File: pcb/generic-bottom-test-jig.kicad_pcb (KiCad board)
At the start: 2 copper layers, 36 x 36 mm, 13 parts

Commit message: Gerbers for v1 of the test jig.
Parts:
- removed PORT_ANDOR1: SN74LVC1G0832, Housings_SOT-23_SOT-143_TSOT-6:SC-70-6_Handsoldering
- removed PORT_C1: 0.1uF, Capacitors_SMD:C_0603_HandSoldering
- removed PORT_IC1: AT24CS02-MAHM, Housings_DFN_QFN:DFN-8-1EP_3x2mm_Pitch0.5mm
- removed PORT_IN1: DF40-80pin-Header, DF40-80pin-Header
- removed PORT_INV1, PORT_XOR1: SN74LVC1G58, Housings_SOT-23_SOT-143_TSOT-6:SC-70-6_Handsoldering
- removed PORT_P1: CONN_01X01, Measurement_Points:Measurement_Point_Round-SMD-Pad_Small
- removed PORT_R1: 10k, Resistors_SMD:R_0603_HandSoldering
- added C1: 2.2uF, Capacitors_SMD:C_0603_HandSoldering, F.Cu at (110.6, 106.4)
- added C2: 1uF, Capacitors_SMD:C_0603_HandSoldering, F.Cu at (116.9, 106.4)
- added CON1: BARREL_JACK, barrel-jack:PJ-037BH-SMT, F.Cu at (116.5, 118.5)
- added D1: RED, LEDs:LED_0603, F.Cu at (125.2, 134.3)
- added D2: YELLOW, LEDs:LED_0603, F.Cu at (125.2, 130.8)
- added D3: GREEN, LEDs:LED_0603, F.Cu at (125.2, 127.3)
- added G***: Chickadee 3mm, chickadee:chickadee_3mm_fcu, F.Cu at (159.9, 129.2)
- added G***: LOGO, flightstack:flightstack-12mm, F.Cu at (190.6, 129.5)
- added P1: CONN_01X06, Pin_Headers:Pin_Header_Straight_1x06, F.Cu at (111.1, 138.6)
- added P10: CONN_01X01, Measurement_Points:Measurement_Point_Round-TH_Small, F.Cu at (120.6, 106.3)
- added P11: CONN_01X01, Measurement_Points:Measurement_Point_Square-TH_Small, F.Cu at (119.2, 111.0)
- added P2: CONN_02X25, Pin_Headers:Pin_Header_Straight_2x25, F.Cu at (134.0, 138.6)
- added P3: CONN_01X04, Pin_Headers:Pin_Header_Straight_1x04, F.Cu at (117.2, 97.2)
- added P4: CONN_02X25, Pin_Headers:Pin_Header_Straight_2x25, F.Cu at (134.0, 87.8)
- added P5: CONN_01X16, fci:SFW12LF-16pin, F.Cu at (144.5, 130.0)
- added P6: CONN_02X10, hirose-df40:DF40-1.5mm-20pin-Receptacle, F.Cu at (190.2, 108.0)
- added P7: CONN_01X01, mill-max-pogo-pin:0910, F.Cu at (158.6, 91.2)
- added P8: CONN_01X16, fci:SFW12LF-16pin, F.Cu at (175.0, 130.0)
- added P9: CONN_01X01, Measurement_Points:Measurement_Point_Round-TH_Small, F.Cu at (117.8, 101.8)
- added Q1: Q_NMOS_GSD, TO_SOT_Packages_SMD:SOT-23_Handsoldering, F.Cu at (115.0, 111.0)
- added R1: 1k, Resistors_SMD:R_0603_HandSoldering, F.Cu at (120.3, 134.3)
- added R2: 1k, Resistors_SMD:R_0603_HandSoldering, F.Cu at (120.3, 130.8)
- added R3: 1k, Resistors_SMD:R_0603_HandSoldering, F.Cu at (120.3, 127.3)
- added R4: 0, Resistors_SMD:R_0603_HandSoldering, B.Cu at (118.7, 132.8)
- added R5: 0, Resistors_SMD:R_0603_HandSoldering, B.Cu at (113.6, 132.8)
- added REF**: MountingHole_3mm, Mounting_Holes:MountingHole_3mm, F.Cu at (193.8, 123.2)
- added REF**: MountingHole_3mm, Mounting_Holes:MountingHole_3mm, F.Cu at (193.8, 92.8)
- added SW1: Switch_SPDT_x2, copal-electronics:CL-SB-22B, F.Cu at (113.3, 89.0)
- added SW2: SPST, Buttons_Switches_SMD:SW_SPST_PTS645, F.Cu at (114.0, 130.2)
- added U1: STMPS2151, TO_SOT_Packages_SMD:SOT-23-5, F.Cu at (113.8, 101.8)
- added U2: TLV70233DBV, TO_SOT_Packages_SMD:SOT-23-5, F.Cu at (113.7, 106.3)
- PORT_OUT1: value DF40-3-4mm-80pin-Receptacle -> CKD_SANDWICH; footprint DF40-3-4mm-80pin-Receptacle -> hirose-df40:DF40-3-4mm-80pin-Receptacle
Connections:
- PORT_OUT1 pad 1: (no net) -> /PD5
- PORT_OUT1 pad 10: (no net) -> /PC15
- PORT_OUT1 pad 11: (no net) -> /PB7_SDA
- PORT_OUT1 pad 12: (no net) -> /PB6_SCL
- PORT_OUT1 pad 13: (no net) -> /PF0
- PORT_OUT1 pad 14: (no net) -> /PF1
- PORT_OUT1 pad 15: (no net) -> /PF9
- PORT_OUT1 pad 16: (no net) -> /PC0_3V3
- PORT_OUT1 pad 17: (no net) -> /PC1_3V3_E
- PORT_OUT1 pad 18: (no net) -> /PC2_BATT
- PORT_OUT1 pad 19: (no net) -> /PF10_5V
- PORT_OUT1 pad 2: (no net) -> /PD7
- PORT_OUT1 pad 20: (no net) -> /PF10_5V
- PORT_OUT1 pad 21: (no net) -> /PF10_5V
- PORT_OUT1 pad 22: (no net) -> /PF10_5V
- PORT_OUT1 pad 23: (no net) -> /PF10_5V
- PORT_OUT1 pad 24: (no net) -> /PF10_5V
- PORT_OUT1 pad 25: (no net) -> /PC3_SWITCH
- PORT_OUT1 pad 26: (no net) -> /PF2
- PORT_OUT1 pad 27: (no net) -> /PA1
- PORT_OUT1 pad 28: (no net) -> /PA3
- PORT_OUT1 pad 29: (no net) -> /PA2
- PORT_OUT1 pad 3: (no net) -> /PB4
- PORT_OUT1 pad 30: (no net) -> /PF4
- PORT_OUT1 pad 31: (no net) -> /PA5_SCL
- PORT_OUT1 pad 32: (no net) -> /PA4
- PORT_OUT1 pad 33: (no net) -> /PA7_SDA
- PORT_OUT1 pad 34: (no net) -> /PA6_SDO
- PORT_OUT1 pad 35: (no net) -> /PC5
- PORT_OUT1 pad 36: (no net) -> /PC4
- PORT_OUT1 pad 37: (no net) -> /PB0
- PORT_OUT1 pad 38: (no net) -> /PB1
- PORT_OUT1 pad 39: (no net) -> /PB2
- PORT_OUT1 pad 4: (no net) -> /PB5
- PORT_OUT1 pad 40: (no net) -> /PE7
- PORT_OUT1 pad 41: (no net) -> /PD6
- PORT_OUT1 pad 42: (no net) -> /PD3
- PORT_OUT1 pad 43: (no net) -> /PD4
- PORT_OUT1 pad 44: (no net) -> /PD1
- PORT_OUT1 pad 45: (no net) -> /PD2
- PORT_OUT1 pad 46: (no net) -> /PC12
- PORT_OUT1 pad 47: (no net) -> /PD0
- PORT_OUT1 pad 48: (no net) -> /PC10
- PORT_OUT1 pad 49: (no net) -> /PC11
- PORT_OUT1 pad 5: (no net) -> /PB8
- PORT_OUT1 pad 50: (no net) -> /PA14_SWCLK
- PORT_OUT1 pad 51: (no net) -> /PA15
- PORT_OUT1 pad 52: (no net) -> /PF6
- PORT_OUT1 pad 53: (no net) -> /PA10
- PORT_OUT1 pad 54: (no net) -> /PA9
- PORT_OUT1 pad 55: (no net) -> /PA8
- PORT_OUT1 pad 56: (no net) -> /PC9
- PORT_OUT1 pad 57: (no net) -> /PC8_GND
- PORT_OUT1 pad 58: (no net) -> /PC8_GND
- PORT_OUT1 pad 59: (no net) -> /PC8_GND
- PORT_OUT1 pad 6: (no net) -> /PB9
- PORT_OUT1 pad 60: (no net) -> /PC8_GND
- PORT_OUT1 pad 61: (no net) -> /PC8_GND
- PORT_OUT1 pad 62: (no net) -> /PC8_GND
- PORT_OUT1 pad 63: (no net) -> /PC8_GND
- PORT_OUT1 pad 64: (no net) -> /PC8_GND
- PORT_OUT1 pad 65: (no net) -> /PC6_BOOT0
- PORT_OUT1 pad 66: (no net) -> /PC7_RESET
- PORT_OUT1 pad 67: (no net) -> /PD15
- PORT_OUT1 pad 68: (no net) -> /PD14
- PORT_OUT1 pad 69: (no net) -> /PD13
- PORT_OUT1 pad 7: (no net) -> /PE6
- PORT_OUT1 pad 70: (no net) -> /PD12
- PORT_OUT1 pad 71: (no net) -> /PD11
- PORT_OUT1 pad 72: (no net) -> /PD10
- PORT_OUT1 pad 73: (no net) -> /PD9_RX
- PORT_OUT1 pad 74: (no net) -> /PD8_TX
- PORT_OUT1 pad 75: (no net) -> /PB15
- PORT_OUT1 pad 76: (no net) -> /PB14
- PORT_OUT1 pad 77: (no net) -> /PB13
- PORT_OUT1 pad 78: (no net) -> /PB12
- PORT_OUT1 pad 79: (no net) -> /PB11
- PORT_OUT1 pad 8: (no net) -> /PC13
- PORT_OUT1 pad 80: (no net) -> /PB10
- PORT_OUT1 pad 9: (no net) -> /PC14
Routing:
- net (no net): track 470.7 -> 0.07 mm, vias 78 -> 0
- net /PC8_GND: track 0.00 -> 157.4 mm, vias 0 -> 2
- net /PF10_5V: track 0.00 -> 131.7 mm, vias 0 -> 4
- net /PC7_RESET: track 0.00 -> 126.9 mm, vias 0 -> 6
- net /PC0_3V3: track 0.00 -> 98.9 mm, vias 0 -> 1
- net /PE9_LD3_RED: track 0.00 -> 93.2 mm, vias 0 -> 4
- net /PC6_BOOT0: track 0.00 -> 86.0 mm, vias 0 -> 4
- net +5V: track 0.00 -> 85.5 mm, vias 0 -> 4
- net /PA13_SWDIO: track 0.00 -> 82.4 mm, vias 0 -> 1
- net /PC3_SWITCH: track 0.00 -> 78.5 mm, vias 0 -> 2
- net /SWCLK: track 0.00 -> 78.2 mm, vias 0 -> 7
- net /PE11_LD7_GREEN: track 0.00 -> 71.3 mm, vias 0 -> 3
- net /SWDIO: track 0.00 -> 70.4 mm, vias 0 -> 7
- net /PC2_BATT: track 0.00 -> 69.3 mm, vias 0 -> 2
- net /PE10_LD5_ORANGE: track 0.00 -> 66.4 mm, vias 0 -> 4
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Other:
- board size 36 x 36 mm -> 88.5 x 56.8 mm
- net class Default: clearance 0.1524 -> 0.14986
- net class Power added: clearance 0.14986, trace_width 0.254, via_dia 0.6858, via_drill 0.3302
- rule trace_clearance: 0.1524 -> 0.14986
- board text added: "3.3V"
- board text added: "3.5mm"
- board text added: "5V"
- board text added: "BUSY"
- board text added: "Expansions Go Here"
- board text added: "FAIL"
- board text added: "Flash"
- board text added: "Flight Controllers Go Here"
- board text added: "GND"
- board text added: "GO"
- board text added: "PASS"
- board text added: "Run"
- board text added: "This side intentionally left blank. (Its the back.)"
- board text added: "ckd.tech/g-test-bot/v1"

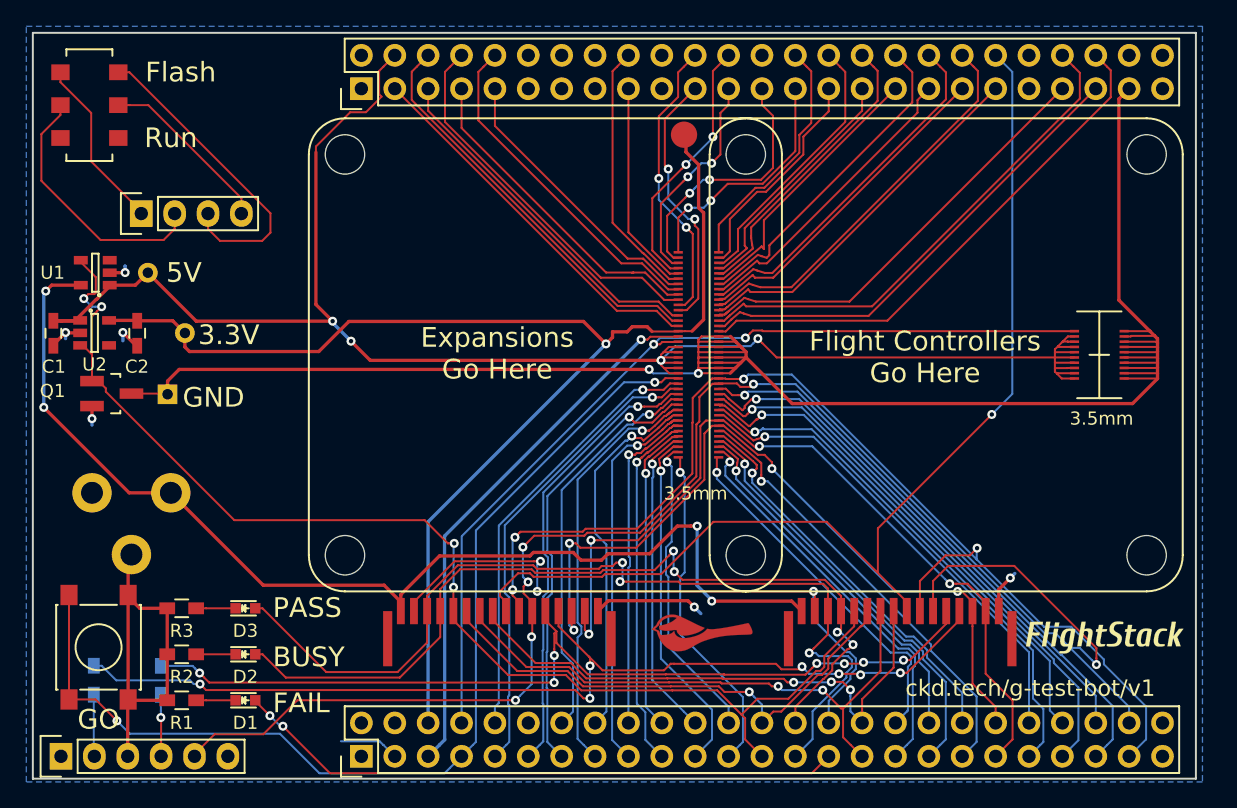
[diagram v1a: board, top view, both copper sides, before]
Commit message: Generic Test Jig Bottom v2 with many changes.
* Stops sharing power enable funcitonality with addressing.
* Fixes power connector footprint.
* Uses a switch to fully change SWD target.
* Stops using PF0 and PF1 which are connected to the shared oscillator which prevent stable height pins.
* Moves the barrel connector to allow the debug board to fit.
* Adds a voltage divider to the current pin on the power connector.
* Adds fiducials.
* Adds OSHW logo.
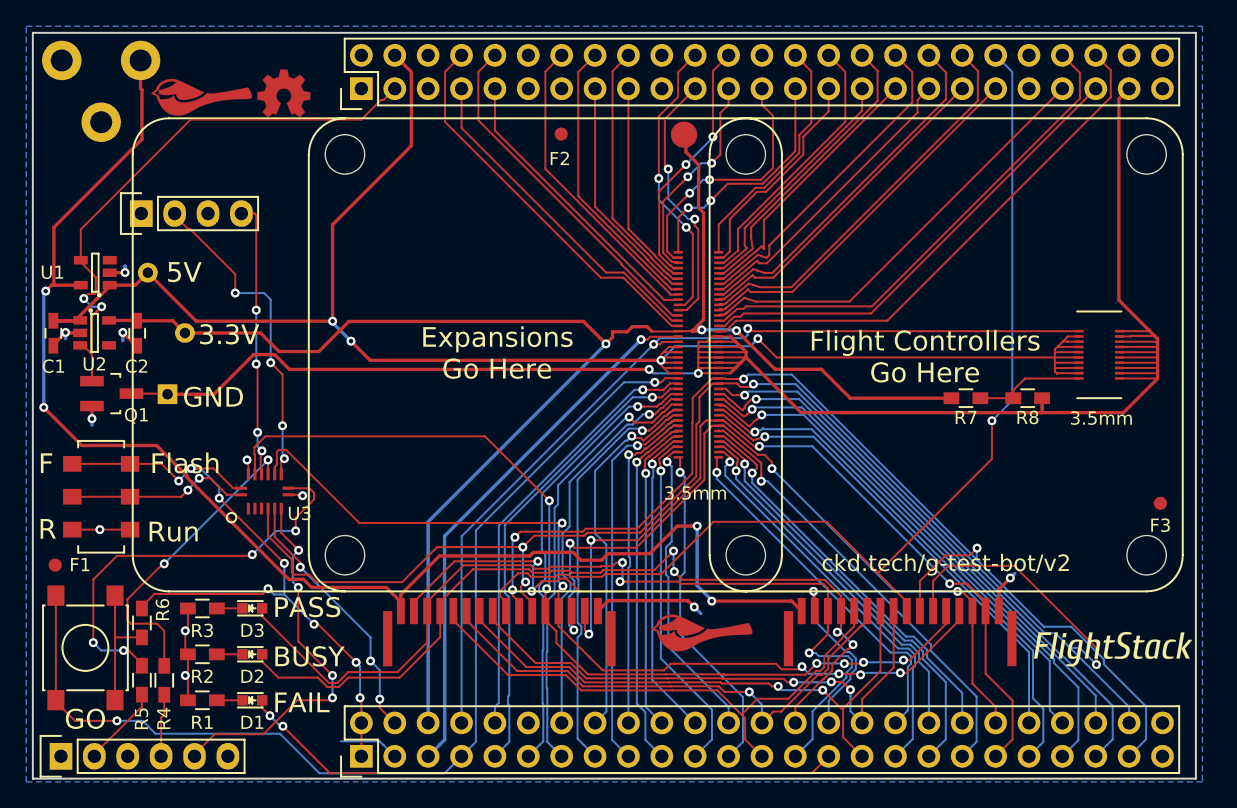
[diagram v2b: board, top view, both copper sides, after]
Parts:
- removed the G*** at (190.6, 129.5)
- added F1: 1mm, macrofab:Fiducial, F.Cu at (110.7, 124.0)
- added F2: 1mm, macrofab:Fiducial, F.Cu at (149.2, 91.2)
- added F3: 1mm, macrofab:Fiducial, F.Cu at (194.8, 119.3)
- added G***: Chickadee 3mm, chickadee:chickadee_3mm_fcu, F.Cu at (121.8, 88.4)
- added G***: LOGO, flightstack:flightstack_thin-12mm, F.Cu at (191.2, 130.4)
- added G***: OSHW, oshw:oshw-4mm, F.Cu at (128.1, 88.1)
- added R6: 220, Resistors_SMD:R_0603_HandSoldering, F.Cu at (117.3, 128.4)
- added R7: 10k, Resistors_SMD:R_0603_HandSoldering, F.Cu at (180.0, 111.3)
- added R8: 10k, Resistors_SMD:R_0603_HandSoldering, F.Cu at (184.7, 111.3)
- added U3: 74LS257, nxp:SOT763-1(DHVQFN16), F.Cu at (126.7, 118.4)
- R4, R5: moved to F.Cu
- moved CON1 33.0 mm to (114.2, 85.6)
- moved SW1 29.8 mm to (114.2, 118.8)
- moved R5 3.66 mm to (117.3, 132.8)
- moved R3 1.57 mm to (121.9, 127.3)
- moved R1 1.57 mm to (121.9, 134.3)
- moved R2 1.57 mm to (121.9, 130.8)
- moved SW2 1.00 mm to (113.0, 130.3)
- moved D1 0.53 mm to (125.7, 134.3)
- moved D2 0.52 mm to (125.7, 130.8)
- moved D3 0.52 mm to (125.7, 127.3)
- moved R4 0.26 mm to (119.0, 132.8)
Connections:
- net Net-(P2-Pad12) renamed /PA0
- net Net-(P4-Pad11) renamed /PE4
- net Net-(P4-Pad12) renamed /PE5
- net Net-(P4-Pad13) renamed /PE2
- C1 pad 2: GNDPWR -> GND
- C2 pad 2: GNDPWR -> GND
- CON1 pad 2: GNDPWR -> GND
- CON1 pad 3: GNDPWR -> GND
- P1 pad 3: GNDPWR -> GND
- P1 pad 5: /PC7_RESET -> /nRST
- P2 pad 1: Net-(P2-Pad1) -> VCC
- P2 pad 2: Net-(P2-Pad2) -> VCC
- P2 pad 3: GNDPWR -> GND
- P2 pad 4: Net-(P2-Pad4) -> /HOST_nRST
- P2 pad 49: GNDPWR -> GND
- P2 pad 50: GNDPWR -> GND
- P3 pad 2: Net-(P3-Pad2) -> /HOST_SWCLK
- P3 pad 4: Net-(P3-Pad4) -> /HOST_SWDIO
- P4 pad 14: Net-(P4-Pad14) -> /PE3
- P4 pad 15: Net-(P4-Pad15) -> /PE0
- P4 pad 16: Net-(P4-Pad16) -> /PE1
- P4 pad 3: /PF9 -> /PF9_POWER_ENABLE
- P4 pad 49: GNDPWR -> GND
- P4 pad 5: /PF0 -> Net-(P4-Pad5)
- P4 pad 50: GNDPWR -> GND
- P4 pad 6: /PF1 -> Net-(P4-Pad6)
- P5 pad 12: /SWDIO -> /TEST_SWDIO
- P5 pad 13: /SWCLK -> /TEST_SWCLK
- P5 pad 16: GNDPWR -> GND
- P6 pad 1: /PF10_5V -> Net-(P6-Pad1)
- P8 pad 12: /SWDIO -> /TEST_SWDIO
- P8 pad 13: /SWCLK -> /TEST_SWCLK
- P8 pad 16: GNDPWR -> GND
- PORT_OUT1 pad 10: /PC15 -> /PE6
- PORT_OUT1 pad 13: /PF0 -> /PC13
- PORT_OUT1 pad 14: /PF1 -> /PC14
- PORT_OUT1 pad 15: /PF9 -> /PC15
- PORT_OUT1 pad 7: /PE6 -> /PE0
- PORT_OUT1 pad 8: /PC13 -> /PE1
- PORT_OUT1 pad 9: /PC14 -> /PE3
- Q1 pad 1: /PE9_LD3_RED -> /PF9_POWER_ENABLE
- Q1 pad 2: GNDPWR -> GND
- R1 pad 2: GNDPWR -> GND
- R2 pad 2: GNDPWR -> GND
- R3 pad 2: GNDPWR -> GND
- SW1 pad 1: Net-(P3-Pad1) -> VCC
- SW1 pad 2: Net-(P3-Pad2) -> /SWD_SELECT
- SW1 pad 3: Net-(SW1-Pad3) -> GND
- SW1 pad 4: Net-(P3-Pad3) -> VCC
- SW1 pad 5: Net-(P3-Pad4) -> /SWD_SELECT
- SW1 pad 6: Net-(SW1-Pad6) -> GND
- SW2 pad 2: GNDPWR -> Net-(R6-Pad2)
- U1 pad 2: GNDPWR -> GND
- U1 pad 4: /PE9_LD3_RED -> /PF9_POWER_ENABLE
- U2 pad 2: GNDPWR -> GND
- U2 pad 3: /PE9_LD3_RED -> /PF9_POWER_ENABLE
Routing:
- net /TEST_SWDIO: track 0.00 -> 71.4 mm, vias 0 -> 6
- net /TEST_SWCLK: track 0.00 -> 69.3 mm, vias 0 -> 6
- net VCC: track 0.00 -> 54.0 mm, vias 0 -> 8
- net GNDPWR: track 53.7 -> 0.00 mm, vias 6 -> 0
- net /PE9_LD3_RED: track 93.2 -> 42.4 mm, vias 4 -> 0
- net /SWDIO: track 70.4 -> 23.6 mm, vias 7 -> 2
- net /SWCLK: track 78.2 -> 31.9 mm, vias 7 -> 4
- net /PF9_POWER_ENABLE: track 0.00 -> 43.5 mm, vias 0 -> 2
- net GND: track 0.00 -> 38.7 mm, vias 0 -> 11
- net /PF1: track 31.2 -> 0.00 mm
- net /PF9: track 29.0 -> 0.00 mm
- net /nRST: track 0.00 -> 28.8 mm, vias 0 -> 4
- net /PF0: track 27.2 -> 0.00 mm
- net /HOST_SWCLK: track 0.00 -> 24.8 mm, vias 0 -> 4
- net Net-(P3-Pad3): track 24.1 -> 0.00 mm
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- added copper zone on B.Cu, net GND
- removed copper zone on B.Cu, net GNDPWR
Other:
- board text added: "F"
- board text added: "R"
- board text added: "ckd.tech/g-test-bot/v2"
- board text removed: "ckd.tech/g-test-bot/v1"

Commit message: Updates to the bottom test jig and addiitonal functionality in runner.
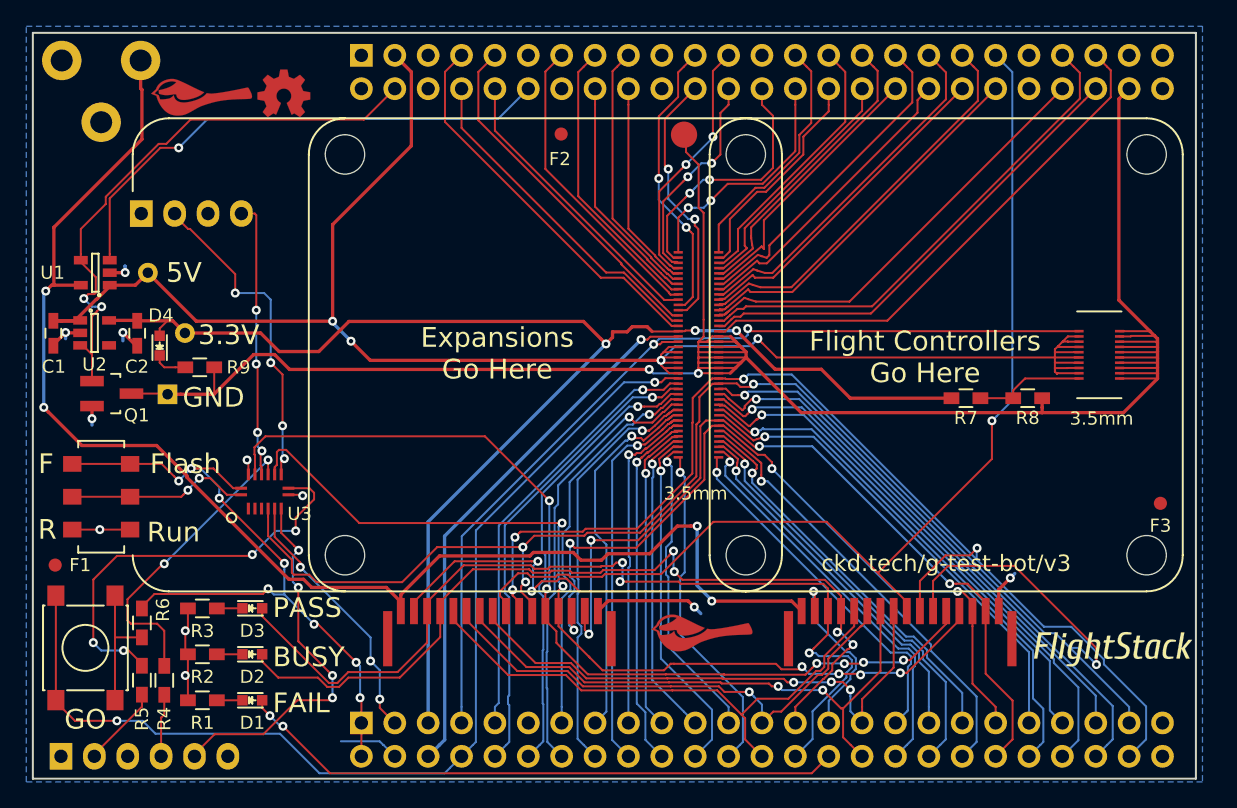
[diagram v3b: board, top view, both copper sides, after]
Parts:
- added D4: RED, LEDs:LED_0603, F.Cu at (118.7, 107.3)
- added R9: 1k, Resistors_SMD:R_0603_HandSoldering, F.Cu at (121.7, 109.0)
- P1, P2, P3, P4: moved to B.Cu
- moved P2 2.54 mm to (134.0, 136.0), turned to 270 degrees
- moved P4 2.54 mm to (134.0, 85.2), turned to 270 degrees
- turned P1 to 270 degrees
- turned P3 to 270 degrees
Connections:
- P2 pad 10: /PF2 -> /PA1
- P2 pad 11: /PA3 -> /PA0
- P2 pad 12: /PA0 -> /PA3
- P2 pad 13: /PF4 -> /PA2
- P2 pad 14: /PA2 -> /PF4
- P2 pad 15: /PA5_SCL -> /PA4
- P2 pad 16: /PA4 -> /PA5_SCL
- P2 pad 17: /PA7_SDA -> /PA6_SDO
- P2 pad 18: /PA6_SDO -> /PA7_SDA
- P2 pad 19: /PC5 -> /PC4
- P2 pad 20: /PC4 -> /PC5
- P2 pad 21: /PB1 -> /PB0
- P2 pad 22: /PB0 -> /PB1
- P2 pad 23: /PE7 -> /PB2
- P2 pad 24: /PB2 -> /PE7
- P2 pad 25: /PE9_LD3_RED -> /PE8_LD4_BLUE
- P2 pad 26: /PE8_LD4_BLUE -> /PE9_LD3_RED
- P2 pad 27: /PE11_LD7_GREEN -> /PE10_LD5_ORANGE
- P2 pad 28: /PE10_LD5_ORANGE -> /PE11_LD7_GREEN
- P2 pad 29: /PE13_LD10_RED -> /PE12_LD9_BLUE
- P2 pad 3: GND -> /HOST_nRST
- P2 pad 30: /PE12_LD9_BLUE -> /PE13_LD10_RED
- P2 pad 31: /PE15_LD6_GREEN -> /PE14_LD8_ORANGE
- P2 pad 32: /PE14_LD8_ORANGE -> /PE15_LD6_GREEN
- P2 pad 33: /PB11 -> /PB10
- P2 pad 34: /PB10 -> /PB11
- P2 pad 35: /PB13 -> /PB12
- P2 pad 36: /PB12 -> /PB13
- P2 pad 37: /PB15 -> /PB14
- P2 pad 38: /PB14 -> /PB15
- P2 pad 39: /PD9_RX -> /PD8_TX
- P2 pad 4: /HOST_nRST -> GND
- P2 pad 40: /PD8_TX -> /PD9_RX
- P2 pad 41: /PD11 -> /PD10
- P2 pad 42: /PD10 -> /PD11
- P2 pad 43: /PD13 -> /PD12
- P2 pad 44: /PD12 -> /PD13
- P2 pad 45: /PD15 -> /PD14
- P2 pad 46: /PD14 -> /PD15
- P2 pad 47: /PC6_BOOT0 -> /PC7_RESET
- P2 pad 48: /PC7_RESET -> /PC6_BOOT0
- P2 pad 5: /PC1_3V3_E -> /PC0_3V3
- P2 pad 6: /PC0_3V3 -> /PC1_3V3_E
- P2 pad 7: /PC3_SWITCH -> /PC2_BATT
- P2 pad 8: /PC2_BATT -> /PC3_SWITCH
- P2 pad 9: /PA1 -> /PF2
- P4 pad 10: /PC13 -> /PE6
- P4 pad 11: /PE4 -> /PE5
- P4 pad 12: /PE5 -> /PE4
- P4 pad 13: /PE2 -> /PE3
- P4 pad 14: /PE3 -> /PE2
- P4 pad 15: /PE0 -> /PE1
- P4 pad 16: /PE1 -> /PE0
- P4 pad 17: /PB8 -> /PB9
- P4 pad 18: /PB9 -> /PB8
- P4 pad 21: /PB6_SCL -> /PB7_SDA
- P4 pad 22: /PB7_SDA -> /PB6_SCL
- P4 pad 23: /PB4 -> /PB5
- P4 pad 24: /PB5 -> /PB4
- P4 pad 25: /PD7 -> /PB3_SWO
- P4 pad 26: /PB3_SWO -> /PD7
- P4 pad 27: /PD5 -> /PD6
- P4 pad 28: /PD6 -> /PD5
- P4 pad 29: /PD3 -> /PD4
- P4 pad 3: /PF9_POWER_ENABLE -> /PF10_5V
- P4 pad 30: /PD4 -> /PD3
- P4 pad 31: /PD1 -> /PD2
- P4 pad 32: /PD2 -> /PD1
- P4 pad 33: /PC12 -> /PD0
- P4 pad 34: /PD0 -> /PC12
- P4 pad 35: /PC10 -> /PC11
- P4 pad 36: /PC11 -> /PC10
- P4 pad 37: /PA14_SWCLK -> /PA15
- P4 pad 38: /PA15 -> /PA14_SWCLK
- P4 pad 39: /PF6 -> /PA13_SWDIO
- P4 pad 4: /PF10_5V -> /PF9_POWER_ENABLE
- P4 pad 40: /PA13_SWDIO -> /PF6
- P4 pad 43: /PA10 -> /PA9
- P4 pad 44: /PA9 -> /PA10
- P4 pad 45: /PA8 -> /PC9
- P4 pad 46: /PC9 -> /PA8
- P4 pad 47: /PC8_GND -> Net-(P4-Pad47)
- P4 pad 48: Net-(P4-Pad48) -> /PC8_GND
- P4 pad 7: /PC14 -> /PC15
- P4 pad 8: /PC15 -> /PC14
- P4 pad 9: /PE6 -> /PC13
- P7 pad 1: /PC0_3V3 -> /PC8_GND
- U1 pad 3: Net-(U1-Pad3) -> /PE4
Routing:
- net /PE4: track 0.00 -> 40.0 mm, vias 0 -> 1
- net /PC8_GND: track 162.8 -> 181.4 mm
- net /PC0_3V3: track 120.2 -> 106.1 mm
- net Net-(D4-Pad1): track 0.00 -> 2.65 mm
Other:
- board text added: "ckd.tech/g-test-bot/v3"
- board text removed: "ckd.tech/g-test-bot/v2"
